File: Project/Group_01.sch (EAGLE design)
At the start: 29 parts, among them J1 POWER_JACKPTH_LOCK, U1 +12v, U3 TCA9546A, U4 TMUX1208

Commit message: Revert "Changed name"
This reverts commit 609342ddda2755176251b6021189b0587eea2b8d.
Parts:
- renumbered U3 to U$3
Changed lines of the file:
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@@
 <setting verticaltext="up"/>
 </settings>
-<grid distance="0.1" unitdist="inch" unit="inch" style="lines" multiple="1" display="no" altdistance="0.01" altunitdist="inch" altunit="inch"/>
+<grid distance="0.1" unitdist="mm" unit="mm" style="lines" multiple="1" display="no" altdistance="0.01" altunitdist="inch" altunit="inch"/>
 <layers>
 <layer number="1" name="Top" color="4" fill="1" visible="no" active="no"/>
@@
 <part name="SUPPLY6" library="SparkFun-PowerSymbols" library_urn="urn:adsk.eagle:library:530" deviceset="5V" device=""/>
 <part name="SUPPLY7" library="SparkFun-PowerSymbols" library_urn="urn:adsk.eagle:library:530" deviceset="5V" device=""/>
-<part name="U3" library="Group_01_Library" deviceset="TCA9546A" device=""/>
+<part name="U$3" library="Group_01_Library" deviceset="TCA9546A" device=""/>
 <part name="GND5" library="SparkFun-PowerSymbols" library_urn="urn:adsk.eagle:library:530" deviceset="GND" device=""/>
 <part name="GND6" library="SparkFun-PowerSymbols" library_urn="urn:adsk.eagle:library:530" deviceset="GND" device=""/>
@@
 <attribute name="VALUE" x="104.14" y="-50.546" size="1.778" layer="96" align="bottom-center"/>
 </instance>
-<instance part="U3" gate="G$1" x="106.68" y="-88.9" smashed="yes">
+<instance part="U$3" gate="G$1" x="106.68" y="-88.9" smashed="yes">
 <attribute name="NAME" x="96.52" y="-66.04" size="1.778" layer="95"/>
 <attribute name="VALUE" x="93.98" y="-114.3" size="1.778" layer="96"/>
@@
 <pinref part="GND5" gate="1" pin="GND"/>
 <wire x1="83.82" y1="-109.22" x2="83.82" y2="-106.68" width="0.1524" layer="91"/>
-<pinref part="U3" gate="G$1" pin="GND"/>
+<pinref part="U$3" gate="G$1" pin="GND"/>
 <wire x1="83.82" y1="-106.68" x2="88.9" y2="-106.68" width="0.1524" layer="91"/>
 </segment>
 <segment>
 <pinref part="GND7" gate="1" pin="GND"/>
-<pinref part="U3" gate="G$1" pin="!RESET!"/>
+<pinref part="U$3" gate="G$1" pin="!RESET!"/>
 <wire x1="86.36" y1="-81.28" x2="88.9" y2="-81.28" width="0.1524" layer="91"/>
 </segment>
@@
 </segment>
 <segment>
-<pinref part="U3" gate="G$1" pin="VCC"/>
+<pinref part="U$3" gate="G$1" pin="VCC"/>
 <wire x1="127" y1="-55.88" x2="149.86" y2="-55.88" width="0.1524" layer="91"/>
 <wire x1="149.86" y1="-55.88" x2="160.02" y2="-55.88" width="0.1524" layer="91"/>
@@
 <net name="I2C_SCL_0" class="0">
 <segment>
-<pinref part="U3" gate="G$1" pin="SC0"/>
+<pinref part="U$3" gate="G$1" pin="SC0"/>
 <wire x1="66.04" y1="-91.44" x2="88.9" y2="-91.44" width="0.1524" layer="91"/>
 <pinref part="R2" gate="G$1" pin="1"/>
@@
 <pinref part="R3" gate="G$1" pin="1"/>
 <wire x1="73.66" y1="-86.36" x2="73.66" y2="-73.66" width="0.1524" layer="91"/>
-<pinref part="U3" gate="G$1" pin="SD0"/>
+<pinref part="U$3" gate="G$1" pin="SD0"/>
 <wire x1="88.9" y1="-86.36" x2="73.66" y2="-86.36" width="0.1524" layer="91"/>
 <label x="73.66" y="-86.36" size="1.778" layer="95"/>
@@
 <net name="I2C_SDA_1" class="0">
 <segment>
-<pinref part="U3" gate="G$1" pin="SD1"/>
+<pinref part="U$3" gate="G$1" pin="SD1"/>
 <wire x1="88.9" y1="-96.52" x2="50.8" y2="-96.52" width="0.1524" layer="91"/>
 <pinref part="R9" gate="G$1" pin="1"/>
@@
 <pinref part="R8" gate="G$1" pin="1"/>
 <wire x1="38.1" y1="-88.9" x2="38.1" y2="-101.6" width="0.1524" layer="91"/>
-<pinref part="U3" gate="G$1" pin="SC1"/>
+<pinref part="U$3" gate="G$1" pin="SC1"/>
 <wire x1="38.1" y1="-101.6" x2="88.9" y2="-101.6" width="0.1524" layer="91"/>
 <label x="73.66" y="-101.6" size="1.778" layer="95"/>
@@
 <net name="I2C_SDA_2" class="0">
 <segment>
-<pinref part="U3" gate="G$1" pin="SD2"/>
+<pinref part="U$3" gate="G$1" pin="SD2"/>
 <wire x1="124.46" y1="-106.68" x2="180.34" y2="-106.68" width="0.1524" layer="91"/>
 <pinref part="R5" gate="G$1" pin="1"/>
@@
 <pinref part="R4" gate="G$1" pin="1"/>
 <wire x1="170.18" y1="-91.44" x2="170.18" y2="-101.6" width="0.1524" layer="91"/>
-<pinref part="U3" gate="G$1" pin="SC2"/>
+<pinref part="U$3" gate="G$1" pin="SC2"/>
 <wire x1="170.18" y1="-101.6" x2="124.46" y2="-101.6" width="0.1524" layer="91"/>
 <label x="127" y="-101.6" size="1.778" layer="95"/>
@@
 <net name="I2C_SCL_3" class="0">
 <segment>
-<pinref part="U3" gate="G$1" pin="SC3"/>
+<pinref part="U$3" gate="G$1" pin="SC3"/>
 <wire x1="124.46" y1="-91.44" x2="149.86" y2="-91.44" width="0.1524" layer="91"/>
 <pinref part="R6" gate="G$1" pin="1"/>
@@
 <net name="I2C_SDA_3" class="0">
 <segment>
-<pinref part="U3" gate="G$1" pin="SD3"/>
+<pinref part="U$3" gate="G$1" pin="SD3"/>
 <pinref part="R7" gate="G$1" pin="1"/>
 <wire x1="124.46" y1="-96.52" x2="160.02" y2="-96.52" width="0.1524" layer="91"/>
@@
 <net name="I2C_SDA" class="0">
 <segment>
-<pinref part="U3" gate="G$1" pin="SDA"/>
+<pinref part="U$3" gate="G$1" pin="SDA"/>
 <label x="129.54" y="-76.2" size="1.27" layer="95" xref="yes"/>
 <wire x1="124.46" y1="-76.2" x2="129.54" y2="-76.2" width="0.1524" layer="91"/>
@@
 <net name="I2C_SCL" class="0">
 <segment>
-<pinref part="U3" gate="G$1" pin="SCL"/>
+<pinref part="U$3" gate="G$1" pin="SCL"/>
 <label x="129.54" y="-81.28" size="1.27" layer="95" xref="yes"/>
 <wire x1="129.54" y1="-81.28" x2="124.46" y2="-81.28" width="0.1524" layer="91"/>
@@
 <net name="I2C_A2" class="0">
 <segment>
-<pinref part="U3" gate="G$1" pin="A2"/>
+<pinref part="U$3" gate="G$1" pin="A2"/>
 <label x="129.54" y="-86.36" size="1.27" layer="95" xref="yes"/>
 <wire x1="124.46" y1="-86.36" x2="129.54" y2="-86.36" width="0.1524" layer="91"/>
@@
 <net name="I2C_A1" class="0">
 <segment>
-<pinref part="U3" gate="G$1" pin="A1"/>
+<pinref part="U$3" gate="G$1" pin="A1"/>
 <wire x1="88.9" y1="-76.2" x2="86.36" y2="-76.2" width="0.1524" layer="91"/>
 <label x="86.36" y="-76.2" size="1.27" layer="95" rot="R180" xref="yes"/>
@@
 <net name="I2C_A0" class="0">
 <segment>
-<pinref part="U3" gate="G$1" pin="A0"/>
+<pinref part="U$3" gate="G$1" pin="A0"/>
 <wire x1="88.9" y1="-71.12" x2="86.36" y2="-71.12" width="0.1524" layer="91"/>
 <label x="86.36" y="-71.12" size="1.27" layer="95" rot="R180" xref="yes"/>

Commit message: Schematic on 2 sheets
And other minor improvements on the board, added readme file
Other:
- note added: "Microcontroller"
- note added: "Mux"

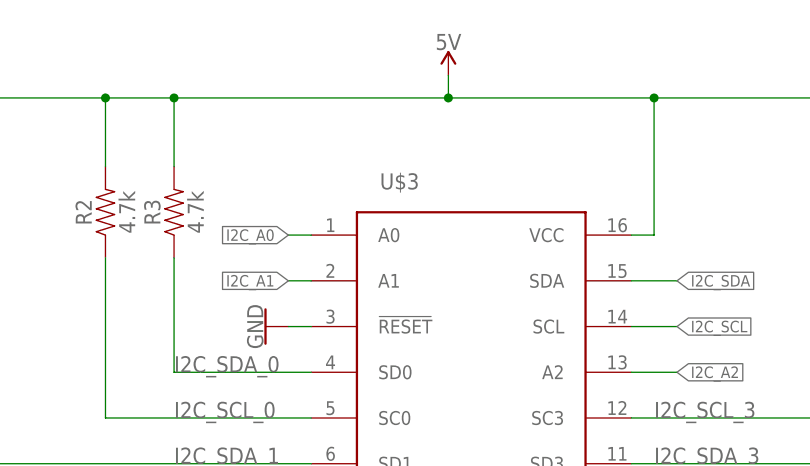
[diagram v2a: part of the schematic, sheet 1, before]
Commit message: Added measure in board
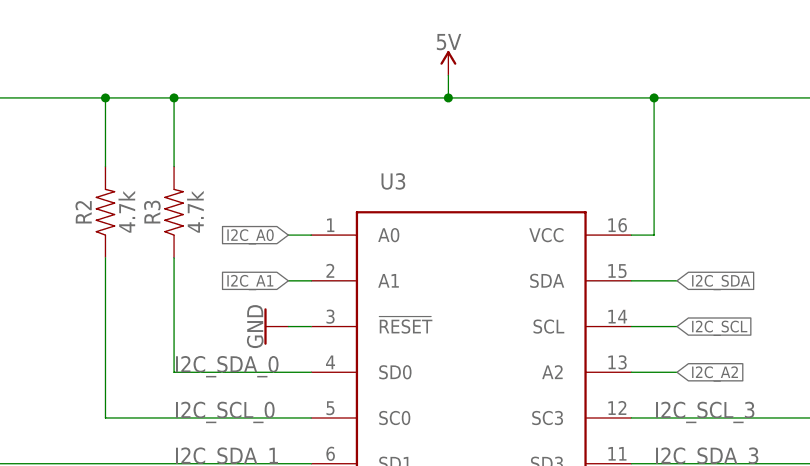
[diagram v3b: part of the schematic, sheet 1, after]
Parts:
- renumbered U$3 to U3
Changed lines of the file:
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@@
 <setting verticaltext="up"/>
 </settings>
-<grid distance="0.1" unitdist="mm" unit="mm" style="lines" multiple="1" display="no" altdistance="0.01" altunitdist="inch" altunit="inch"/>
+<grid distance="0.1" unitdist="inch" unit="inch" style="lines" multiple="1" display="no" altdistance="0.01" altunitdist="inch" altunit="inch"/>
 <layers>
 <layer number="1" name="Top" color="4" fill="1" visible="no" active="no"/>
@@
 <part name="SUPPLY6" library="SparkFun-PowerSymbols" library_urn="urn:adsk.eagle:library:530" deviceset="5V" device=""/>
 <part name="SUPPLY7" library="SparkFun-PowerSymbols" library_urn="urn:adsk.eagle:library:530" deviceset="5V" device=""/>
-<part name="U$3" library="Group_01_Library" deviceset="TCA9546A" device=""/>
+<part name="U3" library="Group_01_Library" deviceset="TCA9546A" device=""/>
 <part name="GND5" library="SparkFun-PowerSymbols" library_urn="urn:adsk.eagle:library:530" deviceset="GND" device=""/>
 <part name="GND6" library="SparkFun-PowerSymbols" library_urn="urn:adsk.eagle:library:530" deviceset="GND" device=""/>
@@
 <attribute name="VALUE" x="87.04" y="167.954" size="1.778" layer="96" align="bottom-center"/>
 </instance>
-<instance part="U$3" gate="G$1" x="89.58" y="129.6" smashed="yes">
+<instance part="U3" gate="G$1" x="89.58" y="129.6" smashed="yes">
 <attribute name="NAME" x="79.42" y="152.46" size="1.778" layer="95"/>
 <attribute name="VALUE" x="76.88" y="104.2" size="1.778" layer="96"/>
@@
 <pinref part="GND5" gate="1" pin="GND"/>
 <wire x1="66.72" y1="109.28" x2="66.72" y2="111.82" width="0.1524" layer="91"/>
-<pinref part="U$3" gate="G$1" pin="GND"/>
+<pinref part="U3" gate="G$1" pin="GND"/>
 <wire x1="66.72" y1="111.82" x2="71.8" y2="111.82" width="0.1524" layer="91"/>
 </segment>
 <segment>
 <pinref part="GND7" gate="1" pin="GND"/>
-<pinref part="U$3" gate="G$1" pin="!RESET!"/>
+<pinref part="U3" gate="G$1" pin="!RESET!"/>
 <wire x1="69.26" y1="137.22" x2="71.8" y2="137.22" width="0.1524" layer="91"/>
 </segment>
@@
 <net name="5V" class="0">
 <segment>
-<pinref part="U$3" gate="G$1" pin="VCC"/>
+<pinref part="U3" gate="G$1" pin="VCC"/>
 <wire x1="109.9" y1="162.62" x2="132.76" y2="162.62" width="0.1524" layer="91"/>
 <wire x1="132.76" y1="162.62" x2="142.92" y2="162.62" width="0.1524" layer="91"/>
@@
 <net name="I2C_SCL_0" class="0">
 <segment>
-<pinref part="U$3" gate="G$1" pin="SC0"/>
+<pinref part="U3" gate="G$1" pin="SC0"/>
 <wire x1="48.94" y1="127.06" x2="71.8" y2="127.06" width="0.1524" layer="91"/>
 <pinref part="R2" gate="G$1" pin="1"/>
@@
 <pinref part="R3" gate="G$1" pin="1"/>
 <wire x1="56.56" y1="132.14" x2="56.56" y2="144.84" width="0.1524" layer="91"/>
-<pinref part="U$3" gate="G$1" pin="SD0"/>
+<pinref part="U3" gate="G$1" pin="SD0"/>
 <wire x1="71.8" y1="132.14" x2="56.56" y2="132.14" width="0.1524" layer="91"/>
 <label x="56.56" y="132.14" size="1.778" layer="95"/>
@@
 <net name="I2C_SDA_1" class="0">
 <segment>
-<pinref part="U$3" gate="G$1" pin="SD1"/>
+<pinref part="U3" gate="G$1" pin="SD1"/>
 <wire x1="71.8" y1="121.98" x2="33.7" y2="121.98" width="0.1524" layer="91"/>
 <pinref part="R9" gate="G$1" pin="1"/>
@@
 <pinref part="R8" gate="G$1" pin="1"/>
 <wire x1="21" y1="129.6" x2="21" y2="116.9" width="0.1524" layer="91"/>
-<pinref part="U$3" gate="G$1" pin="SC1"/>
+<pinref part="U3" gate="G$1" pin="SC1"/>
 <wire x1="21" y1="116.9" x2="71.8" y2="116.9" width="0.1524" layer="91"/>
 <label x="56.56" y="116.9" size="1.778" layer="95"/>
@@
 <net name="I2C_SDA_2" class="0">
 <segment>
-<pinref part="U$3" gate="G$1" pin="SD2"/>
+<pinref part="U3" gate="G$1" pin="SD2"/>
 <wire x1="107.36" y1="111.82" x2="163.24" y2="111.82" width="0.1524" layer="91"/>
 <pinref part="R5" gate="G$1" pin="1"/>
@@
 <pinref part="R4" gate="G$1" pin="1"/>
 <wire x1="153.08" y1="127.06" x2="153.08" y2="116.9" width="0.1524" layer="91"/>
-<pinref part="U$3" gate="G$1" pin="SC2"/>
+<pinref part="U3" gate="G$1" pin="SC2"/>
 <wire x1="153.08" y1="116.9" x2="107.36" y2="116.9" width="0.1524" layer="91"/>
 <label x="109.9" y="116.9" size="1.778" layer="95"/>
@@
 <net name="I2C_SCL_3" class="0">
 <segment>
-<pinref part="U$3" gate="G$1" pin="SC3"/>
+<pinref part="U3" gate="G$1" pin="SC3"/>
 <wire x1="107.36" y1="127.06" x2="132.76" y2="127.06" width="0.1524" layer="91"/>
 <pinref part="R6" gate="G$1" pin="1"/>
@@
 <net name="I2C_SDA_3" class="0">
 <segment>
-<pinref part="U$3" gate="G$1" pin="SD3"/>
+<pinref part="U3" gate="G$1" pin="SD3"/>
 <pinref part="R7" gate="G$1" pin="1"/>
 <wire x1="107.36" y1="121.98" x2="142.92" y2="121.98" width="0.1524" layer="91"/>
@@
 <net name="I2C_SDA" class="0">
 <segment>
-<pinref part="U$3" gate="G$1" pin="SDA"/>
+<pinref part="U3" gate="G$1" pin="SDA"/>
 <label x="112.44" y="142.3" size="1.27" layer="95" xref="yes"/>
 <wire x1="107.36" y1="142.3" x2="112.44" y2="142.3" width="0.1524" layer="91"/>
@@
 <net name="I2C_SCL" class="0">
 <segment>
-<pinref part="U$3" gate="G$1" pin="SCL"/>
+<pinref part="U3" gate="G$1" pin="SCL"/>
 <label x="112.44" y="137.22" size="1.27" layer="95" xref="yes"/>
 <wire x1="112.44" y1="137.22" x2="107.36" y2="137.22" width="0.1524" layer="91"/>
@@
 <net name="I2C_A2" class="0">
 <segment>
-<pinref part="U$3" gate="G$1" pin="A2"/>
+<pinref part="U3" gate="G$1" pin="A2"/>
 <label x="112.44" y="132.14" size="1.27" layer="95" xref="yes"/>
 <wire x1="107.36" y1="132.14" x2="112.44" y2="132.14" width="0.1524" layer="91"/>
@@
 <net name="I2C_A1" class="0">
 <segment>
-<pinref part="U$3" gate="G$1" pin="A1"/>
+<pinref part="U3" gate="G$1" pin="A1"/>
 <wire x1="71.8" y1="142.3" x2="69.26" y2="142.3" width="0.1524" layer="91"/>
 <label x="69.26" y="142.3" size="1.27" layer="95" rot="R180" xref="yes"/>
@@
 <net name="I2C_A0" class="0">
 <segment>
-<pinref part="U$3" gate="G$1" pin="A0"/>
+<pinref part="U3" gate="G$1" pin="A0"/>
 <wire x1="71.8" y1="147.38" x2="69.26" y2="147.38" width="0.1524" layer="91"/>
 <label x="69.26" y="147.38" size="1.27" layer="95" rot="R180" xref="yes"/>
@@
 </sheet>
 </sheets>
-<errors>
-</errors>
 </schematic>
 </drawing>

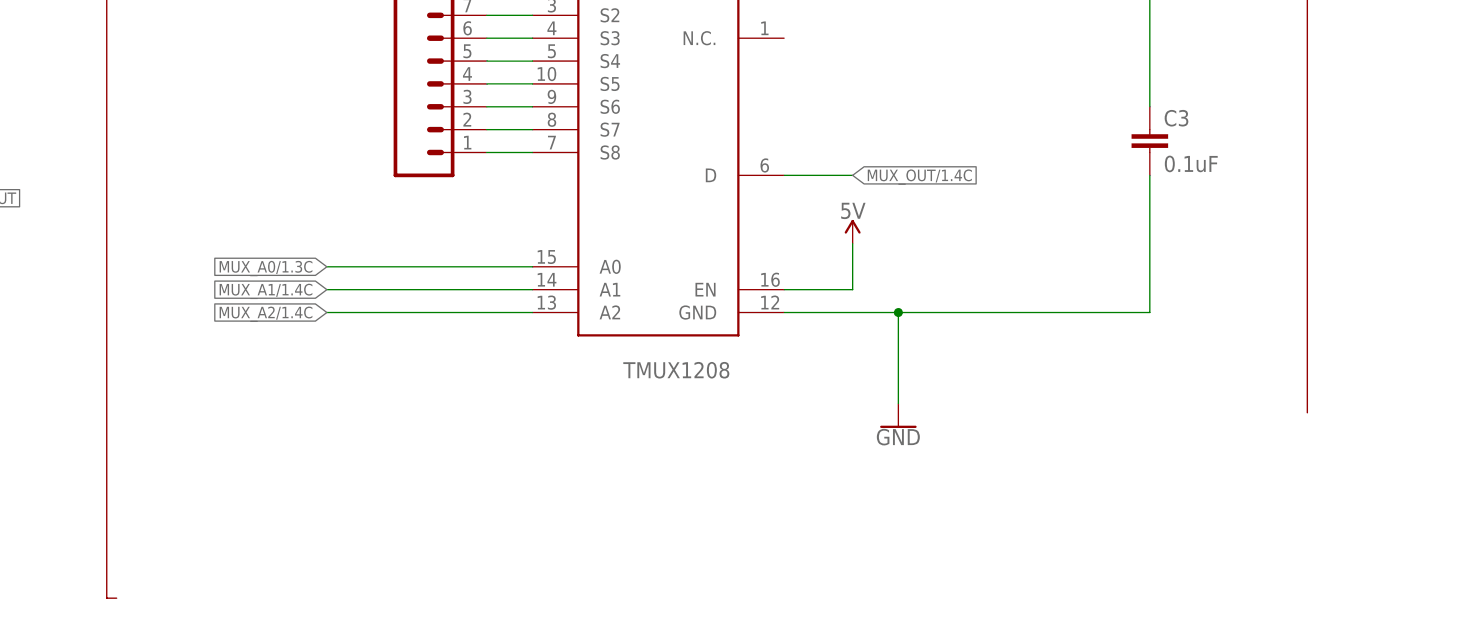
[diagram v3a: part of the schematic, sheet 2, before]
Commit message: Fixed connection between mux and microcontroller
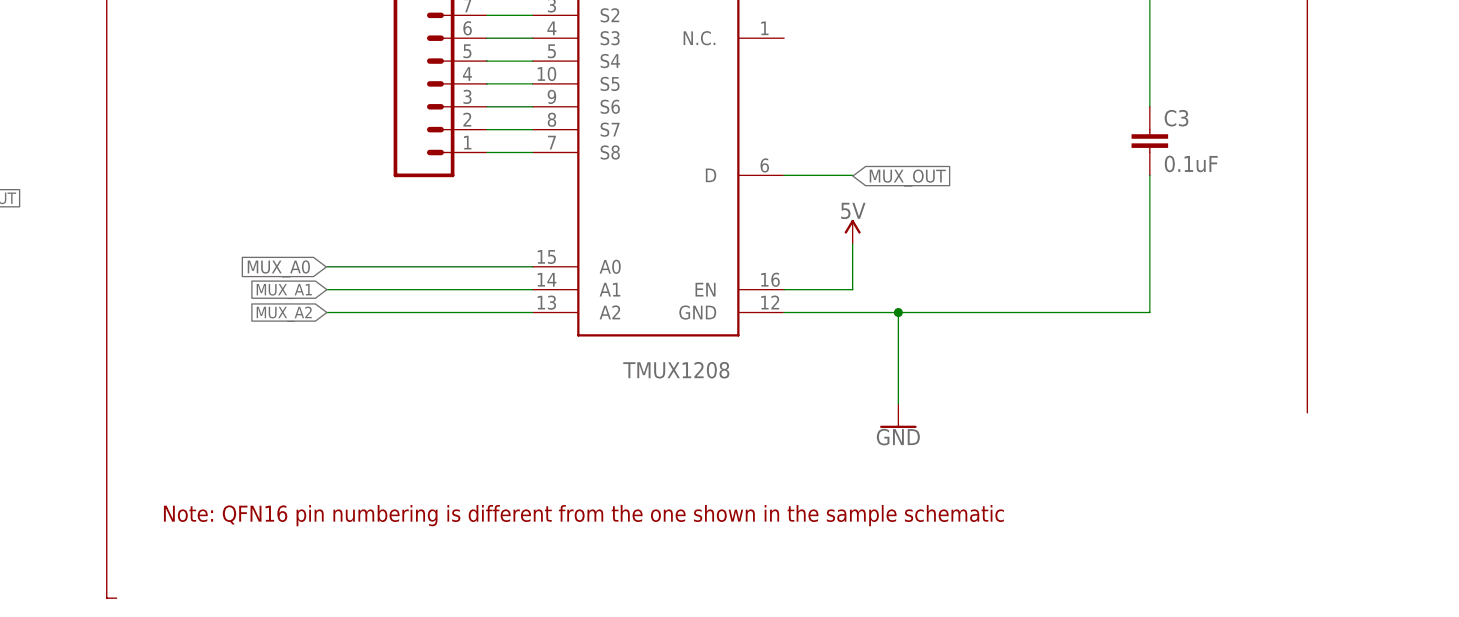
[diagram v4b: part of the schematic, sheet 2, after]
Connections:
- removed net MUX_A0/1.3C: U4.A0
- removed net MUX_A0/2.3C: U$2.P_1.7
- removed net MUX_A1/1.4C: U4.A1
- removed net MUX_A1/2.3C: U$2.P_1.6
- removed net MUX_A2/1.4C: U4.A2
- removed net MUX_A2/2.3C: U$2.P_1.5
- removed net MUX_OUT/1.4C: U4.D
- removed net MUX_OUT/2.5C: U$2.P_1.4
- new net MUX_A0: U$2.P_1.7, U4.A0
- new net MUX_A1: U$2.P_1.6, U4.A1
- new net MUX_A2: U$2.P_1.5, U4.A2
- new net MUX_OUT: U$2.P_1.4, U4.D
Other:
- note added: "Note: QFN16 pin numbering is different from the one shown in the sample schematic"
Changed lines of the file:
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@@
 <setting verticaltext="up"/>
 </settings>
-<grid distance="0.1" unitdist="inch" unit="inch" style="lines" multiple="1" display="no" altdistance="0.01" altunitdist="inch" altunit="inch"/>
+<grid distance="0.1" unitdist="mm" unit="mm" style="lines" multiple="1" display="no" altdistance="0.01" altunitdist="inch" altunit="inch"/>
 <layers>
 <layer number="1" name="Top" color="4" fill="1" visible="no" active="no"/>
@@
 </segment>
 </net>
-<net name="MUX_A0/2.3C" class="0">
+<net name="MUX_A0" class="0">
 <segment>
 <pinref part="U$2" gate="G$1" pin="P_1.7"/>
 <wire x1="97.2" y1="73.72" x2="97.2" y2="81.34" width="0.1524" layer="91"/>
-<label x="97.2" y="81.34" size="1.27" layer="95" rot="R90" xref="yes"/>
-</segment>
-</net>
-<net name="MUX_A1/2.3C" class="0">
+<label x="97.1" y="81.4" size="1.4224" layer="95" rot="R90" xref="yes"/>
+</segment>
+</net>
+<net name="MUX_A1" class="0">
 <segment>
 <pinref part="U$2" gate="G$1" pin="P_1.6"/>
 <wire x1="99.74" y1="73.72" x2="99.74" y2="76.26" width="0.1524" layer="91"/>
-<label x="99.74" y="76.26" size="1.27" layer="95" rot="R90" xref="yes"/>
-</segment>
-</net>
-<net name="MUX_A2/2.3C" class="0">
+<label x="99.7" y="76.3" size="1.4224" layer="95" rot="R90" xref="yes"/>
+</segment>
+</net>
+<net name="MUX_A2" class="0">
 <segment>
 <pinref part="U$2" gate="G$1" pin="P_1.5"/>
 <wire x1="102.28" y1="73.72" x2="102.28" y2="76.26" width="0.1524" layer="91"/>
-<label x="102.28" y="76.26" size="1.27" layer="95" rot="R90" xref="yes"/>
-</segment>
-</net>
-<net name="MUX_OUT/2.5C" class="0">
+<label x="102.3" y="76.3" size="1.4224" layer="95" rot="R90" xref="yes"/>
+</segment>
+</net>
+<net name="MUX_OUT" class="0">
 <segment>
 <pinref part="U$2" gate="G$1" pin="P_1.4"/>
 <wire x1="104.82" y1="73.72" x2="104.82" y2="76.26" width="0.1524" layer="91"/>
-<label x="104.82" y="76.26" size="1.27" layer="95" rot="R90" xref="yes"/>
+<label x="105" y="76.3" size="1.4224" layer="95" rot="R90" xref="yes"/>
 </segment>
 </net>
@@
 <wire x1="193.3" y1="90.1" x2="193.3" y2="24.8" width="0.1524" layer="94"/>
 <text x="68.62" y="82.38" size="2.54" layer="94">Mux</text>
+<text x="66.04" y="12.7" size="1.778" layer="94">Note: QFN16 pin numbering is different from the one shown in the sample schematic</text>
 </plain>
 <instances>
@@
 </segment>
 </net>
-<net name="MUX_A0/1.3C" class="0">
+<net name="MUX_A0" class="0">
 <segment>
 <pinref part="U4" gate="G$1" pin="A0"/>
 <wire x1="107.22" y1="41.02" x2="84.36" y2="41.02" width="0.1524" layer="91"/>
-<label x="84.36" y="41.02" size="1.27" layer="95" rot="R180" xref="yes"/>
-</segment>
-</net>
-<net name="MUX_A1/1.4C" class="0">
+<label x="84.3" y="41" size="1.4224" layer="95" rot="R180" xref="yes"/>
+</segment>
+</net>
+<net name="MUX_A1" class="0">
 <segment>
 <pinref part="U4" gate="G$1" pin="A1"/>
@@
 </segment>
 </net>
-<net name="MUX_A2/1.4C" class="0">
+<net name="MUX_A2" class="0">
 <segment>
 <pinref part="U4" gate="G$1" pin="A2"/>
@@
 </segment>
 </net>
-<net name="MUX_OUT/1.4C" class="0">
+<net name="MUX_OUT" class="0">
 <segment>
 <pinref part="U4" gate="G$1" pin="D"/>
 <wire x1="135.16" y1="51.18" x2="142.78" y2="51.18" width="0.1524" layer="91"/>
-<label x="142.78" y="51.18" size="1.27" layer="95" xref="yes"/>
+<label x="142.8" y="51.1" size="1.4224" layer="95" xref="yes"/>
 </segment>
 </net>
@@
 </sheet>
 </sheets>
+<errors>
+</errors>
 </schematic>
 </drawing>
